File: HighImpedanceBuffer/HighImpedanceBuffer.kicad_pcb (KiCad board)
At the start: 4 copper layers, 110 x 61 mm, 64 parts, among them J1 PJ-102AH, J2 1776540, U1 TPS7A4901DGNR, U2 TPS7A3001DGNR, U3 OPA192IDR, U4 OPA192IDR

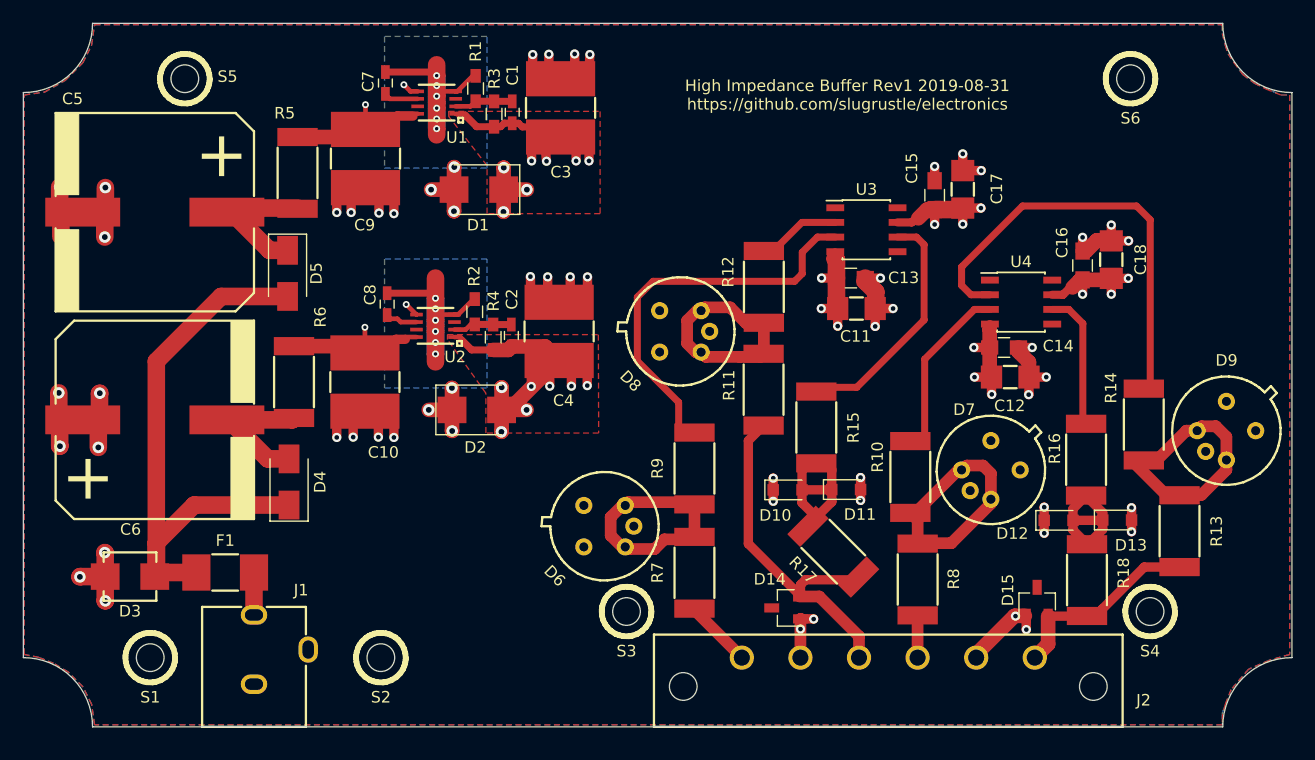
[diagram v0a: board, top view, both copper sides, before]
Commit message: mechanical update
Extended edge of board with connectors 0.8mm so the connector faces sit flush with the front of the enclosure.
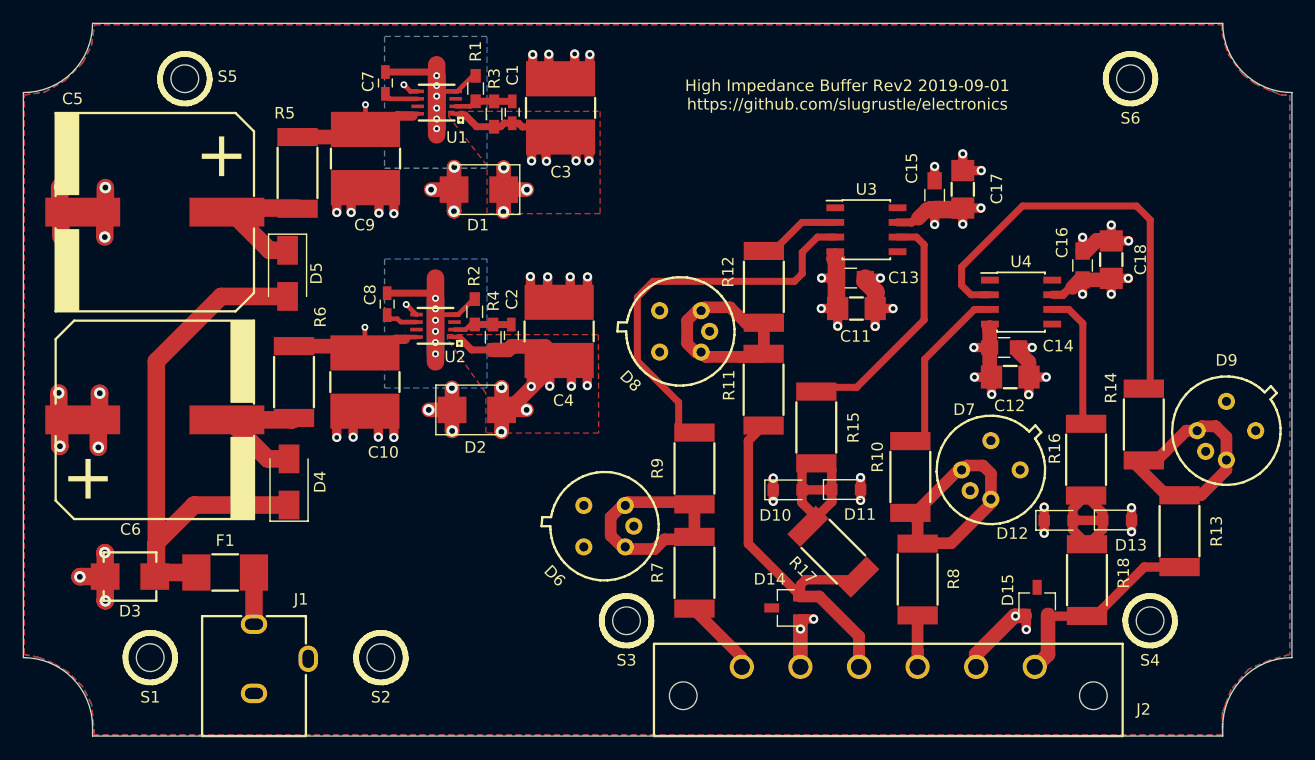
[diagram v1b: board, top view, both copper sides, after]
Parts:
- moved J1 0.80 mm to (120.0, 91.1)
- moved J2 0.80 mm to (175.0, 92.8)
- moved S3 0.80 mm to (152.3, 90.8)
- moved S4 0.80 mm to (197.7, 90.8)
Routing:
- net /OUT1: track 32.1 -> 33.6 mm
- net /IN2: track 3.65 -> 5.11 mm
- net GND: track 204.7 -> 206.0 mm
- net /OUT2: track 17.5 -> 18.4 mm
- net /IN1: track 5.97 -> 6.81 mm
- net Net-(F1-Pad2): track 3.85 -> 4.65 mm
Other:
- board size 110 x 61 mm -> 110 x 61.8 mm
- board text added: "High Impedance Buffer Rev2 2019-09-01 https://github.com/slugrustle/electronics"
- board text removed: "High Impedance Buffer Rev1 2019-08-31 https://github.com/slugrustle/electronics"

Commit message: Rev3, enclosure updates
Rev3: Updating fuse for higher A^2s rating, fixing linear regulator footprint.
Adding enclosure lid & label. Switching to 5/16" long screws for board. Updating diameter of hole for board screws so threads catch better.
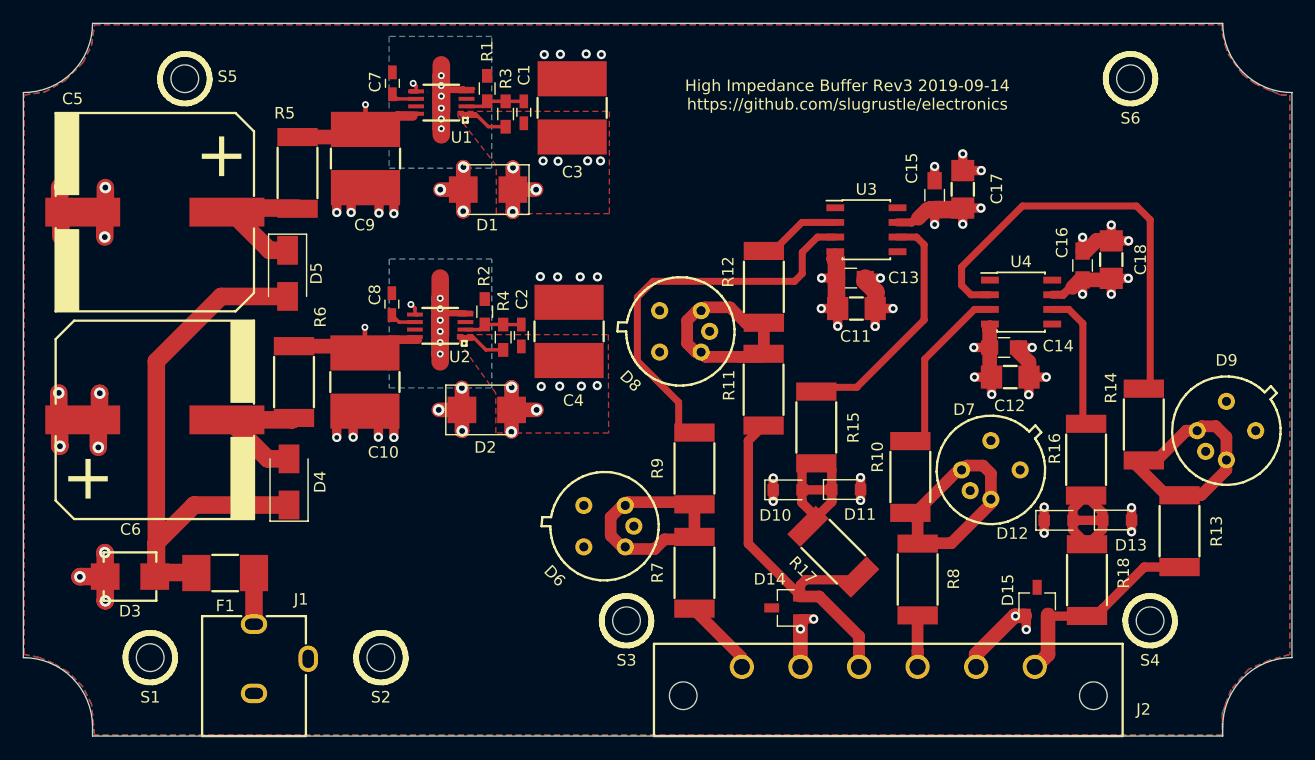
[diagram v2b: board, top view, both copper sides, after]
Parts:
- F1: value 0679L0250-05 -> SF-2410FP0375T-2; footprint HighImpedanceBuffer:0679L -> HighImpedanceBuffer:Fuse_2410
- moved C1 1.00 mm to (143.4, 46.7)
- moved C3 1.00 mm to (147.6, 46.3)
- moved R1 1.00 mm to (140.2, 44.7)
- moved R3 1.00 mm to (141.8, 46.9)
- moved D2 0.86 mm to (140.2, 72.5)
- moved C2 0.86 mm to (143.2, 66.1)
- moved C4 0.86 mm to (147.3, 65.7)
- moved R2 0.86 mm to (140.0, 64.0)
- moved R4 0.86 mm to (141.6, 66.2)
- moved D1 0.80 mm to (140.3, 53.4)
- moved C7 0.61 mm to (132.0, 44.2)
- moved U2 0.41 mm to (136.1, 65.2)
- moved C8 0.41 mm to (132.0, 63.3)
- moved U1 0.40 mm to (136.2, 45.9)
- moved F1 0.05 mm to (117.5, 86.7)
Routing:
- net /18V-: track 65.3 -> 43.7 mm
- net GND: track 206.0 -> 187.3 mm
- net /18V+: track 60.6 -> 45.5 mm
- net /PreReg-: track 20.2 -> 24.0 mm
- net /PreReg+: track 23.4 -> 24.3 mm
- net Net-(C7-Pad1): track 2.99 -> 2.18 mm
- net Net-(C8-Pad1): track 2.82 -> 2.29 mm
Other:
- board text added: "High Impedance Buffer Rev3 2019-09-14 https://github.com/slugrustle/electronics"
- board text removed: "High Impedance Buffer Rev2 2019-09-01 https://github.com/slugrustle/electronics"

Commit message: HighImpedanceBuffer Rev4, SOT23ZenerTester BoM, plate
Improved layout, resistor value changes, and added capacitors to solve oscillation problem in high impedance buffer. Added BoM and CAD for 3D printed support plate to SOT23 Zener Tester.
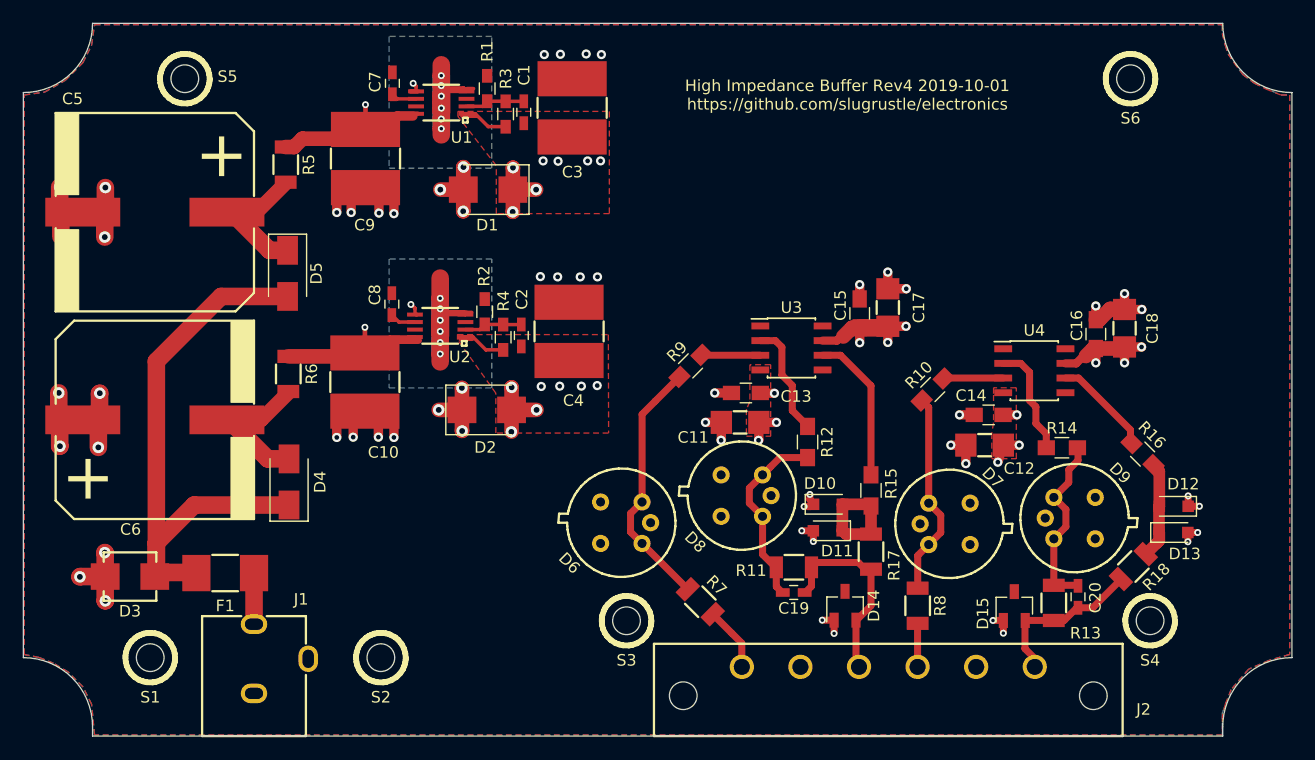
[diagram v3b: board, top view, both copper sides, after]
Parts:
- added C19: TBD, HighImpedanceBuffer:C_0603_HandSoldering, F.Cu at (166.8, 88.3)
- added C20: TBD, HighImpedanceBuffer:C_0603_HandSoldering, F.Cu at (191.4, 88.7)
- R10, R12, R14, R15, R16, R9: footprint HighImpedanceBuffer:R_2512 -> HighImpedanceBuffer:R_0805_HandSoldering
- R11, R13: value 10k -> 2.7k; footprint HighImpedanceBuffer:R_2512 -> HighImpedanceBuffer:R_1206
- R17, R18, R5, R6, R7, R8: footprint HighImpedanceBuffer:R_2512 -> HighImpedanceBuffer:R_1206
- moved R11 15.6 mm to (166.8, 86.2), turned to 180 degrees
- moved D8 15.2 mm to (162.3, 80.0)
- moved D9 15.2 mm to (191.2, 81.9), turned to 135 degrees
- moved C11 14.1 mm to (162.2, 73.6), turned to 180 degrees
- moved R12 14.0 mm to (168.0, 75.3)
- moved C13 13.5 mm to (162.7, 71.0), turned to 180 degrees
- moved R13 12.6 mm to (189.3, 89.2)
- moved C17 12.1 mm to (175.0, 63.6)
- moved U3 12.1 mm to (166.6, 67.1)
- moved C15 12.1 mm to (172.5, 64.1)
- moved D12 10.1 mm to (199.8, 80.9), turned to 180 degrees
- moved R9 8.90 mm to (157.8, 68.7), turned to 225 degrees
- moved R10 7.83 mm to (178.8, 70.8), turned to 225 degrees
- moved R14 7.38 mm to (190.1, 75.8), turned to 0 degrees
- moved R15 7.23 mm to (173.5, 79.5)
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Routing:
- net Net-(R9-Pad1): track 34.7 -> 5.11 mm
- net Net-(R14-Pad1): track 38.1 -> 9.76 mm
- net GND: track 187.3 -> 170.8 mm
- net /OUT1: track 33.6 -> 17.2 mm
- net /18V-: track 43.7 -> 29.7 mm
- net Net-(R10-Pad1): track 15.7 -> 5.16 mm
- net Net-(R15-Pad2): track 21.0 -> 13.0 mm
- net Net-(C20-Pad2): track 23.2 -> 15.8 mm
- net Net-(D10-Pad2): track 16.0 -> 9.86 mm
- net Net-(D12-Pad2): track 13.2 -> 8.35 mm
- net Net-(D7-Pad3): track 22.4 -> 17.8 mm
- net /OUT2: track 18.4 -> 14.3 mm
- net Net-(R16-Pad2): track 12.0 -> 8.55 mm
- net Net-(C19-Pad2): track 19.6 -> 16.4 mm
- net Net-(R12-Pad1): track 7.21 -> 9.85 mm
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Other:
- board text added: "High Impedance Buffer Rev4 2019-10-01 https://github.com/slugrustle/electronics"
- board text removed: "High Impedance Buffer Rev3 2019-09-14 https://github.com/slugrustle/electronics"
